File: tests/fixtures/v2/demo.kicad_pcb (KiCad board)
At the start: 2 copper layers, 30 x 20 mm, 3 parts

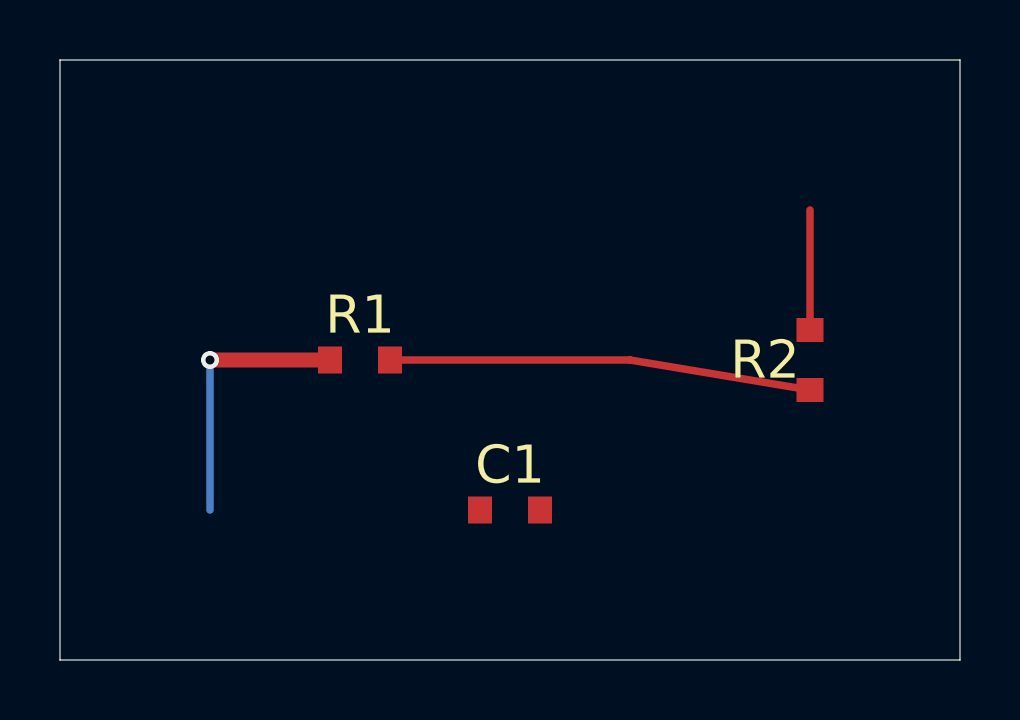
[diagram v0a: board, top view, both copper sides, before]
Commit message: [chore] Detected board change also now covers footprint changes
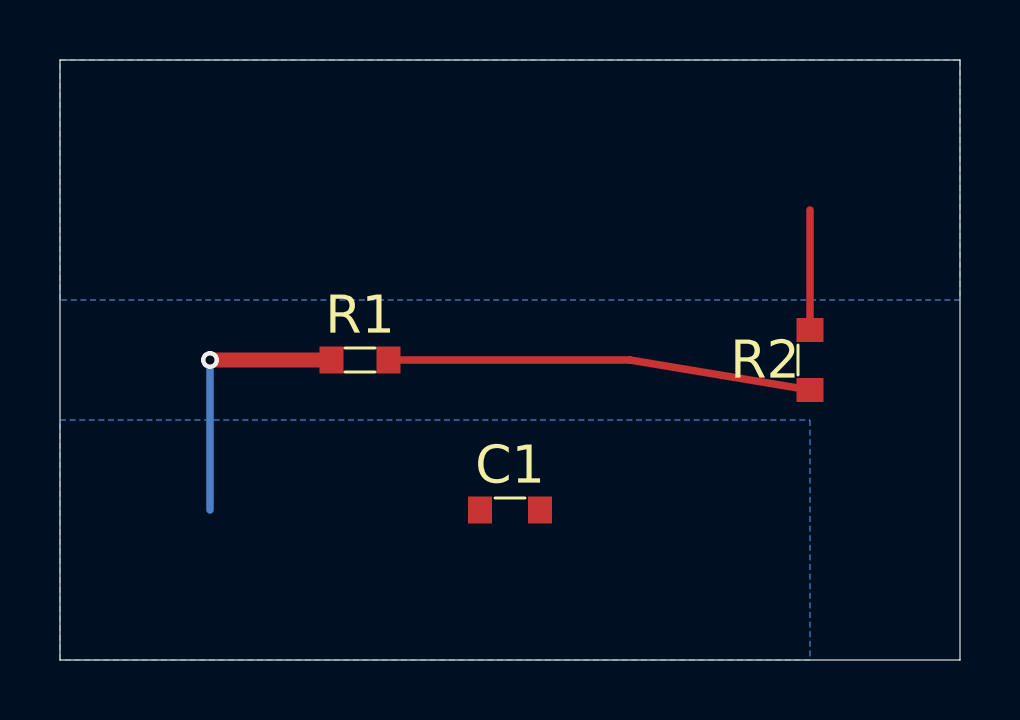
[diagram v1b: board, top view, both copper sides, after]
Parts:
- C1, R1, R2: value (none) -> 1k
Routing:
- added copper zone on B.Cu, net GND
- added copper zone on B.Cu, net VCC
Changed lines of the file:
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@@
 			(layer "F.SilkS")
 		)
+		(property "Value" "1k"
+			(at 0 1.5 0)
+			(layer "F.Fab")
+		)
+		(fp_line
+			(start -0.5 -0.4)
+			(end 0.5 -0.4)
+			(stroke (width 0.1) (type solid))
+			(layer "F.SilkS")
+			(uuid "fp-r1-silk")
+		)
+		(property "Description" "updated footprint"
+			(at 0 0 0)
+			(layer "F.Fab")
+			(hide yes)
+		)
+		(fp_line
+			(start -0.5 0.4)
+			(end 0.5 0.4)
+			(stroke (width 0.1) (type solid))
+			(layer "F.SilkS")
+			(uuid "fp-r1-silk2")
+		)
 		(pad "1" smd rect
-			(at -1 0)
+			(at -0.95 0)
 			(size 0.8 0.9)
 			(layers "F.Cu" "F.Mask")
@@
 		)
 		(pad "2" smd rect
-			(at 1 0)
+			(at 0.95 0)
 			(size 0.8 0.9)
 			(layers "F.Cu" "F.Mask")
@@
 			(at 0 -1.5 0)
 			(layer "F.SilkS")
+		)
+		(property "Value" "1k"
+			(at 0 1.5 0)
+			(layer "F.Fab")
+		)
+		(fp_line
+			(start -0.5 -0.4)
+			(end 0.5 -0.4)
+			(stroke (width 0.1) (type solid))
+			(layer "F.SilkS")
+			(uuid "fp-r2-silk")
 		)
 		(pad "1" smd rect
@@
 		(uuid "via-1")
 	)
+	(zone
+		(net "GND")
+		(layer "B.Cu")
+		(uuid "zone-gnd")
+		(hatch edge 0.5)
+		(connect_pads (clearance 0.5))
+		(min_thickness 0.25)
+		(fill yes (thermal_gap 0.5) (thermal_bridge_width 0.5))
+		(polygon (pts (xy 0 0) (xy 30 0) (xy 30 8) (xy 0 8)))
+	)
+	(zone
+		(net "VCC")
+		(layer "B.Cu")
+		(uuid "zone-vcc")
+		(hatch edge 0.5)
+		(connect_pads (clearance 0.5))
+		(min_thickness 0.25)
+		(fill yes (thermal_gap 0.5) (thermal_bridge_width 0.5))
+		(polygon (pts (xy 0 12) (xy 25 12) (xy 25 20) (xy 0 20)))
+	)
 	(segment
 		(start 5 10)
@@
 			(layer "F.SilkS")
 		)
+		(property "Value" "1k"
+			(at 0 1.5 0)
+			(layer "F.Fab")
+		)
+		(fp_line
+			(start -0.5 -0.4)
+			(end 0.5 -0.4)
+			(stroke (width 0.1) (type solid))
+			(layer "F.SilkS")
+			(uuid "fp-c1-silk")
+		)
 		(pad "1" smd rect
